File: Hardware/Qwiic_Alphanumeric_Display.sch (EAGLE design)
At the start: 33 parts, among them J4 Vertical Qwiic Connector, J5 Vertical Qwiic Connector, U2 XC9140

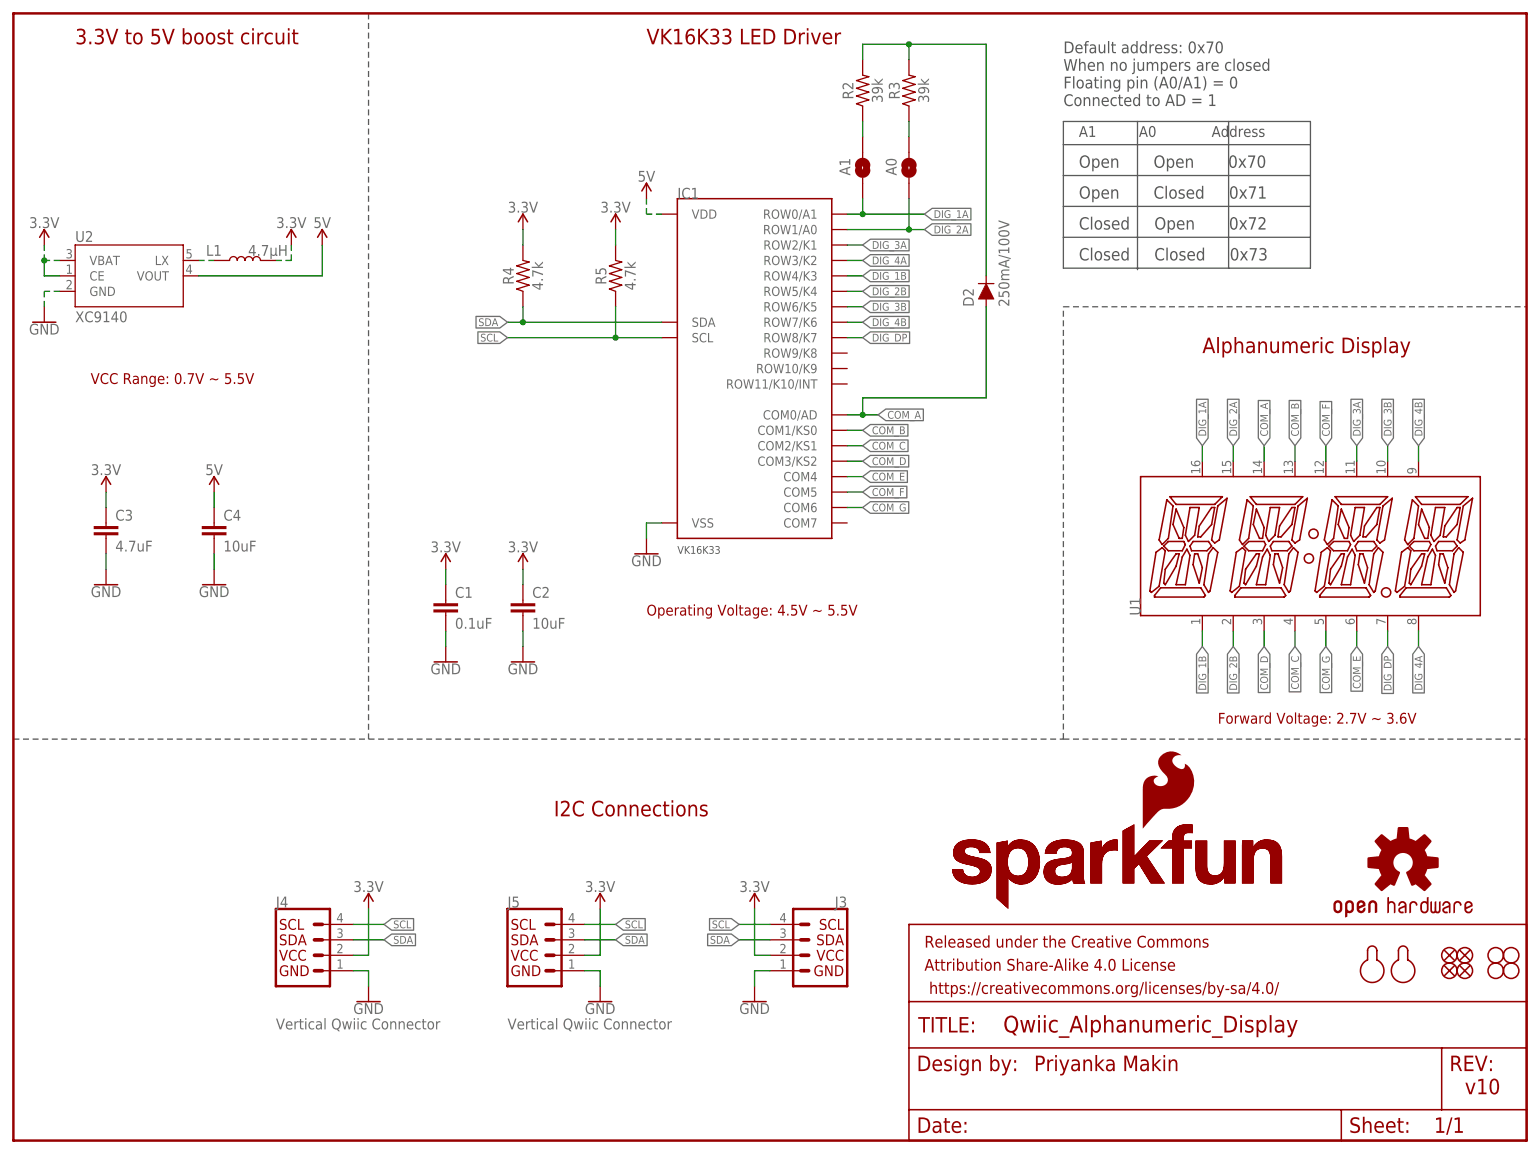
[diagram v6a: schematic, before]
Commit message: Updates from Review:
* Mirrored J3 on sch
* Updated via size so that they're all the same
* Added GND vias near qwiic connectors
* Flipped C1, re-routed
* Moved SDA trace so that copper would flow in dead space (bottom)
* Added I2C jumper and changed pull up resistors to 0402, 1K
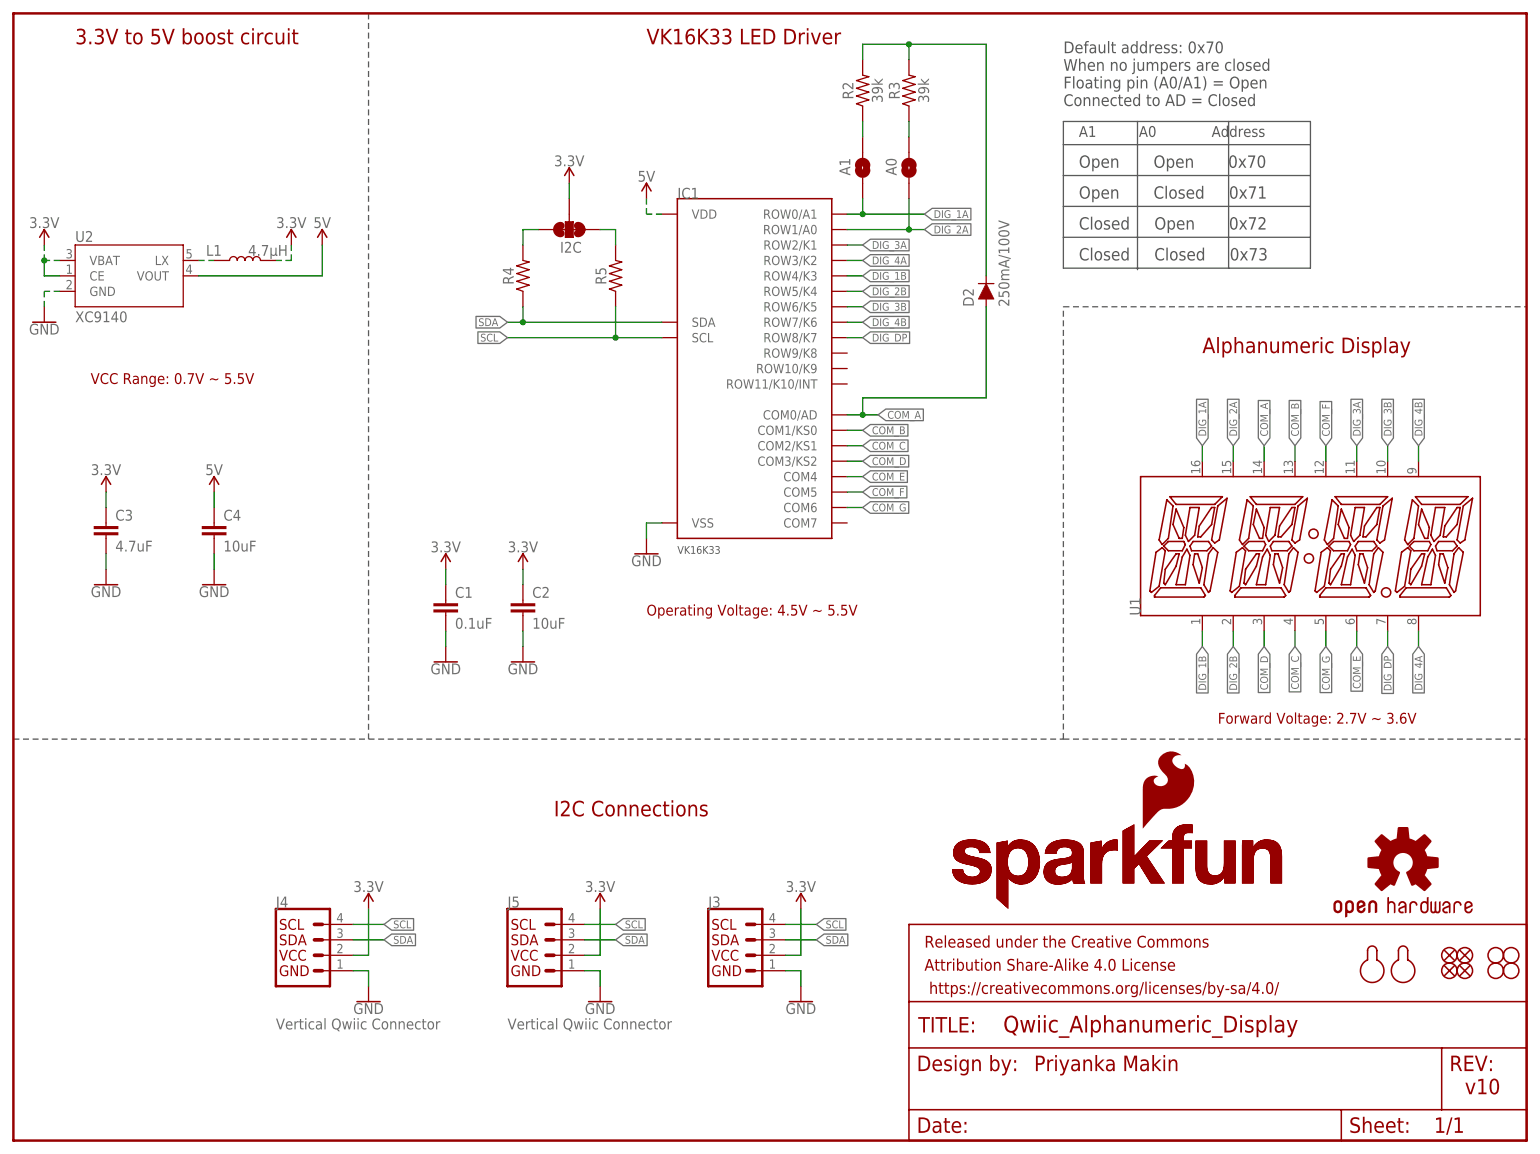
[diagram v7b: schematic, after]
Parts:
- added I2C: JUMPER-SMT_3_2-NC_TRACE_NO-SILK, SparkFun-Jumpers:JUMPER-SMT_3_2-NC_TRACE_NO-SILK
- R4, R5: value 4.7k -> 1KOHM-0402-1/16W-1%; device SparkFun-Resistors:4.7KOHM-0603-1/10W-1% -> SparkFun-Resistors:1KOHM-0402-1/16W-1%
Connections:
- new net N$1: I2C.3, R4.2
- new net N$4: I2C.1, R5.2
- net 3.3V: now also I2C.2; no longer R4.2, R5.2
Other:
- note added: "Default address: 0x70 When no jumpers are closed Floating pin (A0/A1) = Open Connected to AD = Closed"
- note removed: "Default address: 0x70 When no jumpers are closed Floating pin (A0/A1) = 0 Connected to AD = 1"
- moved on the sheet: J3

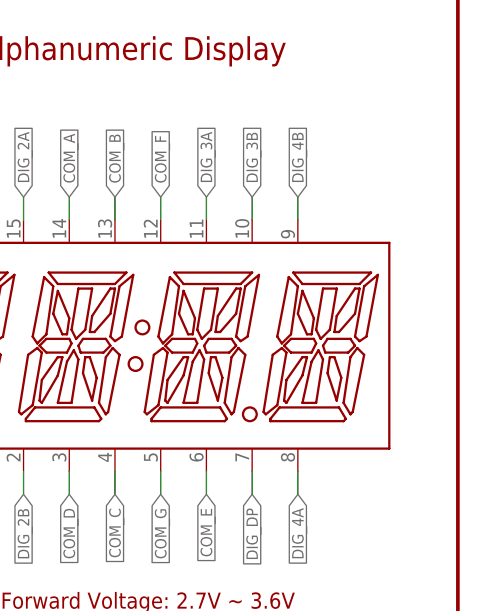
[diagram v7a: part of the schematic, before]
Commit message: QC Double-check updates
* Updated footprint of silsmart display so that pin 1 indicator was in the right place
* Moved fiducials
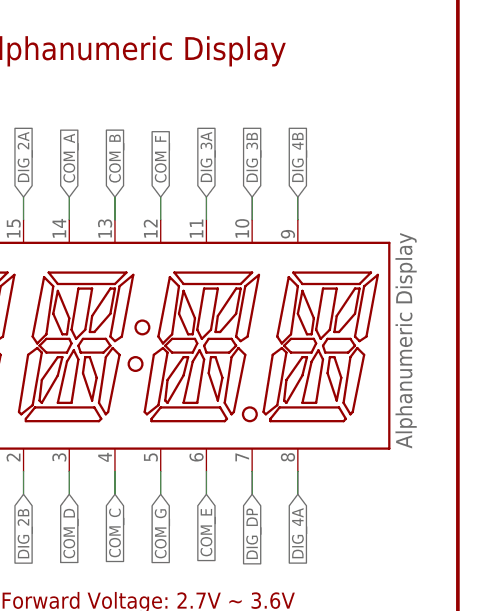
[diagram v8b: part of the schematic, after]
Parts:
- U1: value (none) -> Alphanumeric Display; device Alphanumeric_Display_Library:SILSMART_DISPLAY -> SparkFun-Displays:SILSMART_DISPLAY-PINK
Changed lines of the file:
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@@
 <layer number="154" name="FabDoc2" color="7" fill="1" visible="no" active="no"/>
 <layer number="155" name="FabDoc3" color="7" fill="1" visible="no" active="no"/>
+<layer number="156" name="gesam-Maß" color="1" fill="7" visible="no" active="no"/>
+<layer number="157" name="FaceMchng" color="3" fill="1" visible="no" active="no"/>
+<layer number="158" name="FaceMMeas" color="3" fill="1" visible="no" active="no"/>
+<layer number="159" name="Geh-Bear2" color="1" fill="7" visible="no" active="no"/>
+<layer number="160" name="Topologie" color="9" fill="1" visible="no" active="no"/>
+<layer number="161" name="tomplace2" color="7" fill="1" visible="no" active="no"/>
 <layer number="166" name="AntennaArea" color="7" fill="1" visible="no" active="no"/>
 <layer number="168" name="4mmHeightArea" color="7" fill="1" visible="no" active="no"/>
@@
 <layer number="250" name="Descript" color="3" fill="1" visible="no" active="no"/>
 <layer number="251" name="SMDround" color="12" fill="11" visible="no" active="no"/>
+<layer number="252" name="BR-BS" color="7" fill="1" visible="no" active="no"/>
 <layer number="253" name="Extra" color="7" fill="1" visible="no" active="no"/>
 <layer number="254" name="cooling" color="7" fill="1" visible="no" active="no"/>
@@
 <part name="FD3" library="SparkFun-Aesthetics" deviceset="FIDUCIAL" device="1X2"/>
 <part name="FD4" library="SparkFun-Aesthetics" deviceset="FIDUCIAL" device="1X2"/>
-<part name="U1" library="Alphanumeric_Display_Library" deviceset="SILSMART_DISPLAY" device="">
+<part name="U1" library="SparkFun-Displays" deviceset="SILSMART_DISPLAY" device="-PINK" value="Alphanumeric Display">
 <attribute name="PROD_ID" value="COMP-14892"/>
 </part>
